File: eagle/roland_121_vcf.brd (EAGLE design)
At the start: 100 x 80 mm, 100 parts, among them IC1 TL072P, IC2 LM13700N, IC3 LM13700N, Q1 MPF102, Q2 2N3904, Q3 2N3906, Q4 MPF102, Q5 2N3904, Q6 MPF102, Q7 MPF102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

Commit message: parts on
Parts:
- moved R57 198.4 mm to (92.7, 52.1), turned to 270 degrees
- moved R48 198.3 mm to (80.0, 12.7), turned to 90 degrees
- moved R37 184.6 mm to (77.5, 12.7), turned to 90 degrees
- moved C17 177.7 mm to (83.8, 15.2), turned to 180 degrees
- moved D1 174.7 mm to (72.4, 12.7), turned to 90 degrees
- moved 24DB_OUT 174.7 mm to (95.2, 20.3)
- moved R56 172.7 mm to (73.7, 44.5), turned to 270 degrees
- moved Q7 171.2 mm to (87.6, 52.1), turned to 270 degrees
- moved R38 167.1 mm to (58.4, 36.8), turned to 90 degrees
- moved R47 166.3 mm to (69.8, 48.3), turned to 90 degrees
- moved Q6 165.9 mm to (88.9, 19.1), turned to 180 degrees
- moved R55 164.3 mm to (77.5, 52.1)
- moved Q3 157.5 mm to (54.6, 26.7), turned to 90 degrees
- moved R54 157.3 mm to (77.5, 44.5), turned to 270 degrees
- moved R46 156.9 mm to (64.8, 34.3)
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
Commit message: draft routed
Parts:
- moved R8 20.4 mm to (5.08, 14.0), turned to 90 degrees
- moved FREQ_TRIM 10.2 mm to (7.62, 40.6), turned to 0 degrees
- moved R12 9.25 mm to (8.89, 33.0), turned to 180 degrees
- moved U1 6.48 mm to (15.2, 63.5)
- moved R13 6.35 mm to (17.8, 35.6), turned to 180 degrees
- moved R5 5.68 mm to (8.89, 14.0)
- moved R29 5.39 mm to (17.8, 38.1), turned to 0 degrees
- moved C21 5.24 mm to (5.08, 50.8)
- moved C22 5.24 mm to (16.5, 50.8)
- moved C23 5.24 mm to (10.2, 50.8)
- moved C24 5.24 mm to (21.6, 50.8)
- moved FB1 5.24 mm to (8.89, 55.9)
- moved FB2 5.24 mm to (19.1, 55.9)
- moved IN1 3.81 mm to (14.0, 10.2)
- moved R14 3.81 mm to (6.35, 20.3), turned to 180 degrees
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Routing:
- net GND: track 0.00 -> 360.6 mm
- net -12V: track 0.00 -> 275.4 mm, vias 0 -> 1
- net +12V: track 0.00 -> 269.8 mm, vias 0 -> 2
- net N$16: track 0.00 -> 101.3 mm
- net N$45: track 0.00 -> 99.9 mm, vias 0 -> 1
- net N$55: track 0.00 -> 93.7 mm
- net N$36: track 0.00 -> 79.2 mm
- net N$37: track 0.00 -> 53.8 mm
- net N$23: track 0.00 -> 53.3 mm, vias 0 -> 1
- net N$15: track 0.00 -> 47.1 mm
- net N$8: track 0.00 -> 44.6 mm
- net N$40: track 0.00 -> 42.6 mm, vias 0 -> 1
- net N$35: track 0.00 -> 39.6 mm
- net N$10: track 0.00 -> 36.7 mm, vias 0 -> 1
- net N$42: track 0.00 -> 31.7 mm
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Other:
- board size 100 x 80 mm -> 99.4 x 67.9 mm

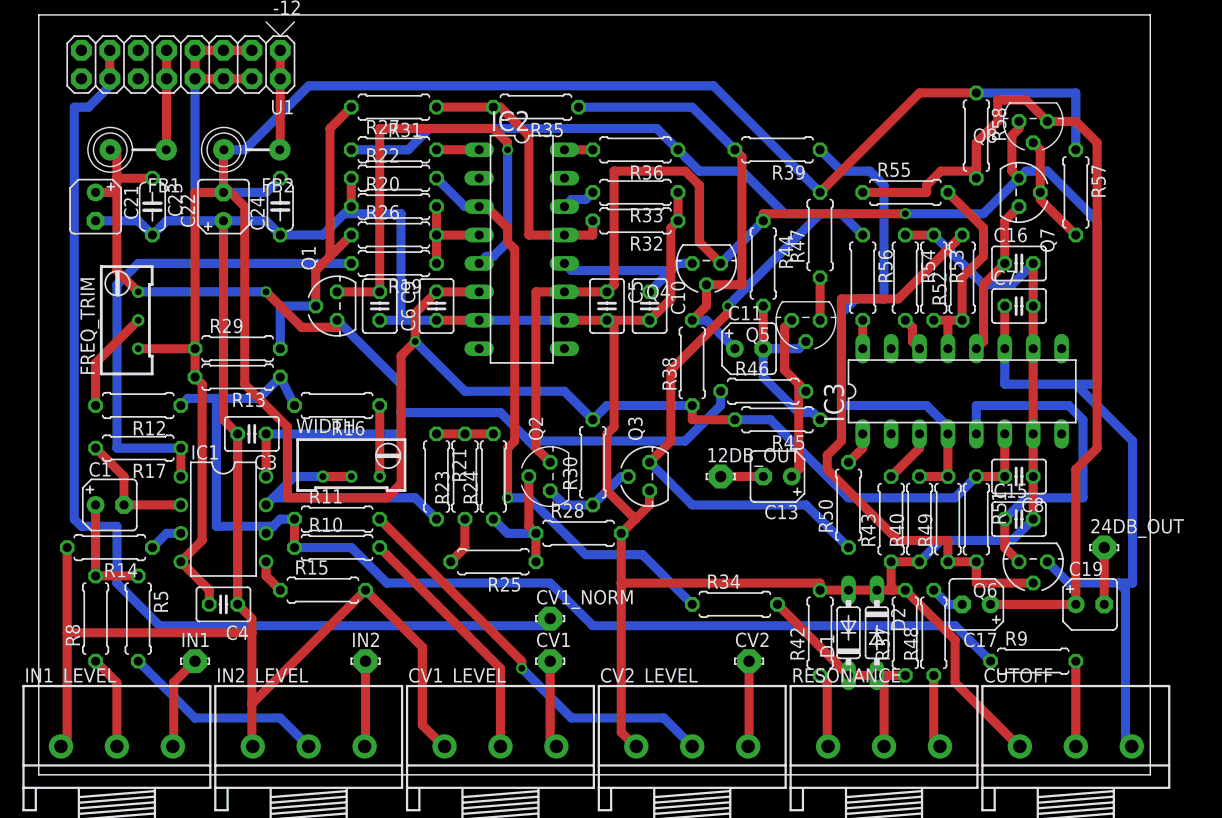
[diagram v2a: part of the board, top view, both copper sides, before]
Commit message: changed FET to 2sk30a
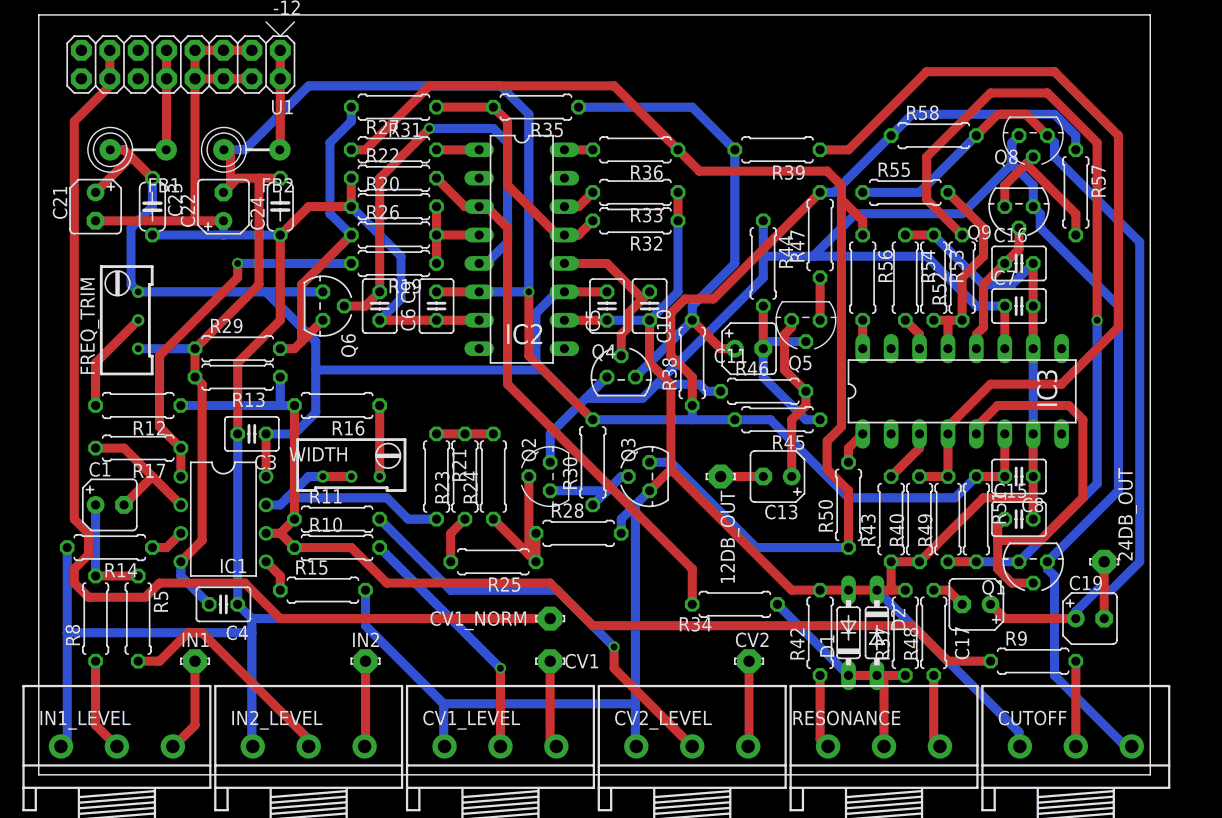
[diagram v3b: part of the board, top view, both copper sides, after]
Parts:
- removed Q7: MPF102, mes_transistors:TO92F
- added Q9: 2SK30, 808:TO92
- Q1, Q4, Q6: value MPF102 -> 2SK30; device mes_transistors:TO92F -> 808:TO92
- moved Q6 67.5 mm to (25.4, 41.9), turned to 270 degrees
- moved Q1 66.3 mm to (88.9, 19.1), turned to 180 degrees
- moved Q4 12.7 mm to (52.1, 35.6), turned to 0 degrees
- moved R58 3.81 mm to (80.0, 57.1), turned to 0 degrees
- moved Q8 1.27 mm to (88.9, 57.1)
- moved 24DB_OUT 1.27 mm to (95.2, 19.1)
- moved C19 1.27 mm to (94.0, 14.0)
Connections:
- net +12V: now also Q9.1; no longer Q7.1
- net N$28: now also Q6.3; no longer Q1.2
- net N$35: now also Q4.3; no longer Q4.2
- net N$37: now also Q1.3; no longer Q6.2
- net N$40: now also Q6.2; no longer Q1.3
- net N$41: now also Q4.2; no longer Q4.3
- net N$42: now also Q1.2; no longer Q6.3
- net N$43: now also Q9.2; no longer Q7.3
- net N$47: now also Q9.3; no longer Q7.2
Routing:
- net -12V: track 275.4 -> 225.9 mm
- net N$15: track 47.1 -> 75.0 mm
- net N$37: track 53.8 -> 74.5 mm, vias 0 -> 1
- net +12V: track 269.8 -> 250.5 mm, vias 2 -> 0
- net N$8: track 44.6 -> 32.9 mm, vias 0 -> 1
- net GND: track 360.6 -> 370.9 mm
- net N$45: track 99.9 -> 108.5 mm, vias 1 -> 0
- net N$16: track 101.3 -> 94.2 mm
- net N$35: track 39.6 -> 44.4 mm
- net N$23: track 53.3 -> 48.7 mm, vias 1 -> 0
- net N$42: track 31.7 -> 36.1 mm
- net N$47: track 9.83 -> 13.7 mm
- net N$40: track 42.6 -> 39.9 mm
- net N$20: track 12.2 -> 14.9 mm
- net N$3: track 25.2 -> 22.6 mm
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
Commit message: ground planes
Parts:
- moved C7 2.54 mm to (90.2, 41.9), turned to 180 degrees
- moved Q5 1.27 mm to (68.6, 39.4), turned to 270 degrees
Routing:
- net GND: track 370.9 -> 0.00 mm
- net N$35: track 44.4 -> 56.8 mm
- net N$40: track 39.9 -> 28.2 mm, vias 1 -> 0
- net N$8: track 32.9 -> 41.3 mm, vias 1 -> 0
- net N$36: track 78.0 -> 85.4 mm, vias 0 -> 1
- net -12V: track 225.9 -> 232.9 mm, vias 1 -> 0
- net N$13: track 22.8 -> 17.9 mm
- net N$15: track 75.0 -> 70.3 mm
- net N$55: track 94.9 -> 91.1 mm
- net N$33: track 17.1 -> 20.9 mm
- net N$42: track 36.1 -> 32.4 mm
- net N$32: track 15.5 -> 12.0 mm
- net +12V: track 250.5 -> 253.8 mm
- net N$16: track 94.2 -> 96.8 mm
- net N$5: track 20.9 -> 18.4 mm
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- added copper zone on layer 1, net GND
- added copper zone on layer 16, net GND
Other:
- board text added: "121 Type VCF"
